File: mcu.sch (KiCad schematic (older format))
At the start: 21 parts, among them J5 CONN_01X03, J6 CONN_01X06, J7 CONN_01X03, SW1 SW_Push, U6 STM32L476RG, Y1 ABS07-120-32.768kHz-T

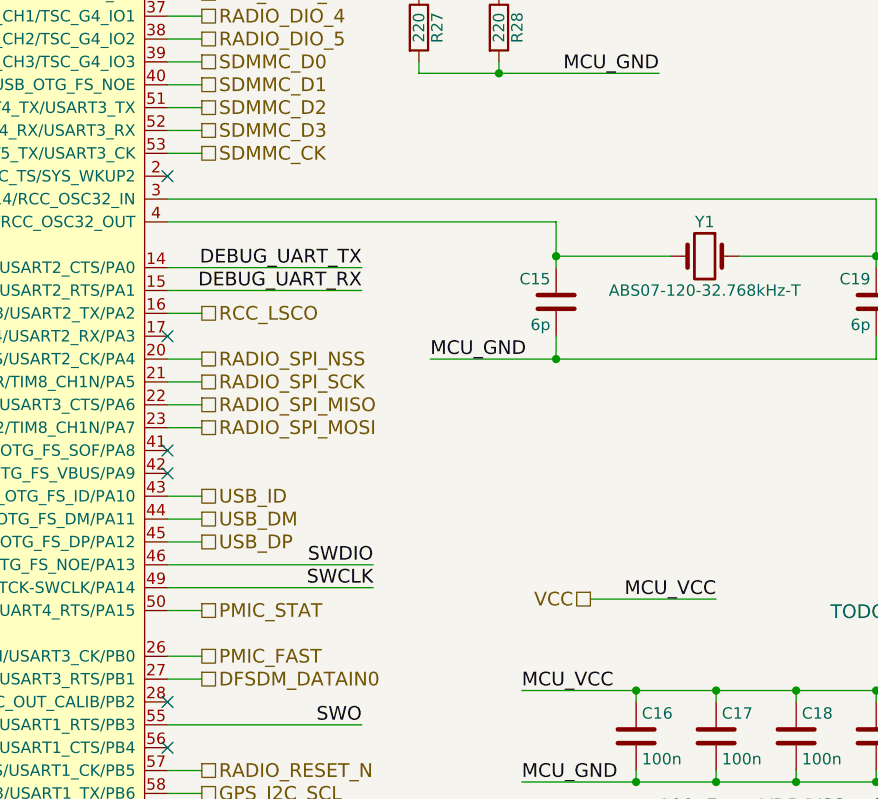
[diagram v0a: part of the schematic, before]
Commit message: Most components arranged on PCB
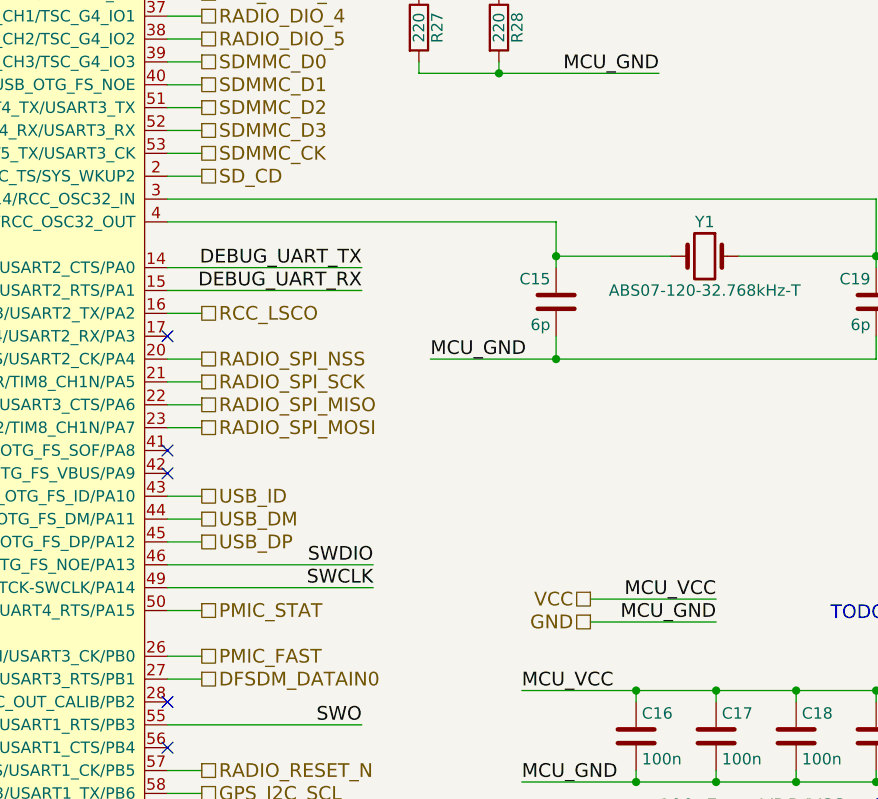
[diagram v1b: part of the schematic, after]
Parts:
- C22: footprint (none) -> Capacitors_SMD:C_0805_HandSoldering
- J6: footprint Pin_Headers:Pin_Header_Straight_1x06_Pitch2.54mm -> tracking_device:Pin_Header_Straight_1x06_Pitch2.54mm
- J7: footprint Pin_Headers:Pin_Header_Straight_1x03_Pitch2.54mm -> tracking_device:Pin_Header_Straight_1x03_Pitch2.54mm
- U6: footprint LQFP64 -> Housings_QFP:LQFP-64_10x10mm_Pitch0.5mm
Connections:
- net MCU_GND is gone; now on net GND: C15.2, C16.2, C17.2, C18.2, C19.2, C20.2, C21.2, C22.2, J5.3 (P3), J7.3 (P3), R26.2, R27.2, R28.2, SW1.2, U6.12 (VSSA), U6.18 (VSS), U6.31 (VSS), U6.47 (VSS), U6.63 (VSS)
- net SD_CD: now reaches U6.2 (PC13/RTC_OUT_ALARM/RTC_OUT_CALIB/RTC_TAMP1/RTC_TS/SYS_WKUP2)
- no-connect marks 14 -> 13
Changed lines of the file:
@@
 LIBS:battery_management
 LIBS:ESD_Protection
+LIBS:u-blox
 LIBS:tracking_device
-LIBS:u-blox
 LIBS:tracking_device-cache
 EELAYER 25 0
@@
 F 0 "J6" H 12150 1650 50  0000 C CNN
 F 1 "CONN_01X06" V 12250 1300 50  0000 C CNN
-F 2 "Pin_Headers:Pin_Header_Straight_1x06_Pitch2.54mm" H 12150 1300 50  0001 C CNN
+F 2 "tracking_device:Pin_Header_Straight_1x06_Pitch2.54mm" H 12150 1300 50  0001 C CNN
 F 3 "" H 12150 1300 50  0001 C CNN
 	1    12150 1300
@@
 F 0 "J7" H 12400 3200 50  0000 C CNN
 F 1 "CONN_01X03" V 12500 3000 50  0000 C CNN
-F 2 "Pin_Headers:Pin_Header_Straight_1x03_Pitch2.54mm" H 12400 3000 50  0001 C CNN
+F 2 "tracking_device:Pin_Header_Straight_1x03_Pitch2.54mm" H 12400 3000 50  0001 C CNN
 F 3 "" H 12400 3000 50  0001 C CNN
 	1    12400 3000
@@
 F 0 "U6" H 700 7450 50  0000 L BNN
 F 1 "STM32L476RG" H 7600 7450 50  0000 R BNN
-F 2 "LQFP64" H 7550 7350 50  0001 R TNN
+F 2 "Housings_QFP:LQFP-64_10x10mm_Pitch0.5mm" H 7550 7350 50  0001 R TNN
 F 3 "" H 3500 4700 50  0001 C CNN
 	1    4200 4400
@@
 F 0 "C22" H 11675 6200 50  0000 L CNN
 F 1 "4.7u" H 11675 6000 50  0000 L CNN
-F 2 "" H 11688 5950 50  0001 C CNN
+F 2 "Capacitors_SMD:C_0805_HandSoldering" H 11688 5950 50  0001 C CNN
 F 3 "" H 11650 6100 50  0001 C CNN
 	1    11650 6100
@@
 NoConn ~ 7850 1850
 NoConn ~ 7850 1950
-NoConn ~ 7850 3650
 NoConn ~ 7850 6150
 Text HLabel 8000 4250 2    60   UnSpc ~ 0
@@
 NoConn ~ 2450 3350
 NoConn ~ 2300 3050
+Text HLabel 8000 3650 2    60   UnSpc ~ 0
+SD_CD
+Wire Wire Line
+	8000 3650 7850 3650
+Text HLabel 9700 5600 0    60   UnSpc ~ 0
+GND
+Text Label 10250 5600 2    60   ~ 0
+MCU_GND
+Wire Wire Line
+	10250 5600 9700 5600
 $EndSCHEMATC

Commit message: Version sent out for fabrication
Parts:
- removed J5: CONN_01X03, Pin_Headers:Pin_Header_Straight_1x03_Pitch2.54mm, symbol CONN_01X03
- renumbered J7 to J10, J6 to J9, R24 to R26, R25 to R27, R26 to R28, R27 to R29, R28 to R30, SW1 to SW3
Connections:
- net PMIC_FAST: now also U6.42 (DAC1_EXTI9/LCD_COM1/TIM15_BKIN/TIM1_CH2/USART1_TX/USB_OTG_FS_VBUS/PA9); no longer U6.26 (ADC1_IN15/ADC2_IN15/COMP1_OUT/LCD_SEG5/OPAMP2_VOUT/QUADSPI_BK1_IO1/TIM1_CH2N/TIM3_CH3/TIM8_CH2N/USART3_CK/PB0)
- net SWITCH_1: now reaches U6.11 (PC3/ADC1_IN4/ADC2_IN4/ADC3_IN4/LCD_VLCD/LPTIM1_ETR/LPTIM2_ETR/SAI1_SD_A/SPI2_MOSI)
- net SWITCH_2: now reaches U6.17 (ADC1_IN8/ADC2_IN8/LCD_SEG2/OPAMP1_VOUT/TIM15_CH2/TIM2_CH4/TIM5_CH4/USART2_RX/PA3)
- net GPS_EXTINT: now reaches U6.28 (COMP1_INP/DFSDM_CKIN0/I2C3_SMBA/LPTIM1_OUT/RTC_OUT_ALARM/RTC_OUT_CALIB/PB2)
- net VUSB_DET: now reaches U6.33 (DFSDM_DATIN1/I2C2_SMBA/LCD_SEG12/LPUART1_DE/LPUART1_RTS/SAI2_FS_A/SPI2_NSS/SWPMI1_IO/TIM15_BKIN/TIM1_BKIN/TIM1_BKIN_COMP2/TSC_G1_IO1/USART3_CK/PB12)
- net GPS_TIMEPULSE: now reaches U6.36 (ADC1_EXTI15/ADC2_EXTI15/ADC3_EXTI15/DFSDM_CKIN2/LCD_SEG15/RTC_REFIN/SAI2_SD_A/SPI2_MOSI/SWPMI1_SUSPEND/TIM15_CH2/TIM1_CH3N/TIM8_CH3N/TSC_G1_IO4/PB15)
- net GPS_RESET_N: now reaches U6.56 (COMP2_INP/LCD_SEG8/SAI1_MCLK_B/SPI1_MISO/SPI3_MISO/SYS_JTRST/TIM17_BKIN/TIM3_CH1/TSC_G2_IO1/UART5_DE/UART5_RTS/USART1_CTS/PB4)
- no-connect marks 13 -> 6
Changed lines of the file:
@@
 LIBS:tracking_device
 LIBS:RF_Modules
+LIBS:Electromechanical
+LIBS:Test_Point
+LIBS:electomech-misc
+LIBS:_electromech
+LIBS:Mounting_Hole
 LIBS:tracking_device-cache
 EELAYER 25 0
@@
 RADIO_SPI_NSS
 $Comp
-L CONN_01X06 J6
+L CONN_01X06 J9
 U 1 1 59A76B28
 P 12150 1300
-F 0 "J6" H 12150 1650 50  0000 C CNN
+F 0 "J9" H 12150 1650 50  0000 C CNN
 F 1 "CONN_01X06" V 12250 1300 50  0000 C CNN
 F 2 "tracking_device:Pin_Header_Straight_1x06_Pitch2.54mm" H 12150 1300 50  0001 C CNN
@@
 $EndComp
 $Comp
-L CONN_01X03 J7
+L CONN_01X03 J10
 U 1 1 59A77202
 P 12400 3000
-F 0 "J7" H 12400 3200 50  0000 C CNN
+F 0 "J10" H 12400 3200 50  0000 C CNN
 F 1 "CONN_01X03" V 12500 3000 50  0000 C CNN
 F 2 "tracking_device:Pin_Header_Straight_1x03_Pitch2.54mm" H 12400 3000 50  0001 C CNN
@@
 Text Label 9000 4450 0    60   ~ 0
 MCU_GND
-$Comp
-L STM32L476RG U6
-U 1 1 59B8C0F3
-P 4200 4400
-F 0 "U6" H 700 7450 50  0000 L BNN
-F 1 "STM32L476RG" H 7600 7450 50  0000 R BNN
-F 2 "Housings_QFP:LQFP-64_10x10mm_Pitch0.5mm" H 7550 7350 50  0001 R TNN
-F 3 "" H 3500 4700 50  0001 C CNN
-	1    4200 4400
-	-1   0    0    -1
-$EndComp
 Text HLabel 8000 3350 2    60   UnSpc ~ 0
 SDMMC_D2
@@
 USB_ID
 $Comp
-L R R25
+L R R27
 U 1 1 59BE1ED5
 P 8800 1350
-F 0 "R25" V 8880 1350 50  0000 C CNN
+F 0 "R27" V 8880 1350 50  0000 C CNN
 F 1 "DNI" V 8800 1350 50  0000 C CNN
 F 2 "Resistors_SMD:R_0805_HandSoldering" V 8730 1350 50  0001 C CNN
@@
 MCU_VCC
 $Comp
-L R R26
+L R R28
 U 1 1 59BE220F
 P 8800 1750
-F 0 "R26" V 8880 1750 50  0000 C CNN
+F 0 "R28" V 8880 1750 50  0000 C CNN
 F 1 "0" V 8800 1750 50  0000 C CNN
 F 2 "Resistors_SMD:R_0805_HandSoldering" V 8730 1750 50  0001 C CNN
@@
 Text Label 8750 5350 2    60   ~ 0
 SWDIO
-$Comp
-L CONN_01X03 J5
-U 1 1 59BE7C26
-P 9250 1550
-F 0 "J5" H 9250 1750 50  0000 C CNN
-F 1 "CONN_01X03" V 9350 1550 50  0000 C CNN
-F 2 "Pin_Headers:Pin_Header_Straight_1x03_Pitch2.54mm" H 9250 1550 50  0001 C CNN
-F 3 "" H 9250 1550 50  0001 C CNN
-	1    9250 1550
-	1    0    0    -1
-$EndComp
 Text HLabel 8000 1650 2    60   UnSpc ~ 0
 VBAT
@@
 	9700 5500 10250 5500
 Wire Wire Line
-	8700 1550 9050 1550
-Wire Wire Line
 	9550 4000 10050 4000
 Wire Wire Line
@@
 Wire Wire Line
 	8800 1950 8800 1900
-Wire Wire Line
-	8800 1150 9050 1150
-Wire Wire Line
-	9050 1150 9050 1450
 Connection ~ 8800 1150
-Wire Wire Line
-	9050 1650 9050 1950
 Wire Wire Line
 	8000 1650 7850 1650
@@
 NoConn ~ 7850 1850
 NoConn ~ 7850 1950
-NoConn ~ 7850 6150
 Text HLabel 8000 4250 2    60   UnSpc ~ 0
 RCC_LSCO
 Wire Wire Line
 	8000 4250 7850 4250
-NoConn ~ 7850 4350
-NoConn ~ 11050 3700
 $Comp
 L LED D2
@@
 $EndComp
 $Comp
-L R R28
+L R R30
 U 1 1 59BF19BB
 P 9300 3000
-F 0 "R28" V 9380 3000 50  0000 C CNN
+F 0 "R30" V 9380 3000 50  0000 C CNN
 F 1 "220" V 9300 3000 50  0000 C CNN
 F 2 "Resistors_SMD:R_0805_HandSoldering" V 9230 3000 50  0001 C CNN
@@
 Wire Wire Line
 	8950 2450 7850 2450
-NoConn ~ 7850 5950
-$Comp
-L R R24
+$Comp
+L R R26
 U 1 1 59BF23D1
 P 8550 1550
-F 0 "R24" V 8630 1550 50  0000 C CNN
+F 0 "R26" V 8630 1550 50  0000 C CNN
 F 1 "10k" V 8550 1550 50  0000 C CNN
 F 2 "Resistors_SMD:R_0805_HandSoldering" V 8480 1550 50  0001 C CNN
@@
 	8000 6250 7850 6250
 $Comp
-L SW_Push SW1
+L SW_Push SW3
 U 1 1 59C0698A
 P 11550 2100
-F 0 "SW1" H 11600 2200 50  0000 L CNN
+F 0 "SW3" H 11600 2200 50  0000 L CNN
 F 1 "SW_Push" H 11550 2040 50  0000 C CNN
 F 2 "Buttons_Switches_THT:SW_PUSH_6mm" H 11550 2300 50  0001 C CNN
@@
 	10950 4450 10950 4350
 $Comp
-L R R27
+L R R29
 U 1 1 59C07A6F
 P 8950 3000
-F 0 "R27" V 9030 3000 50  0000 C CNN
+F 0 "R29" V 9030 3000 50  0000 C CNN
 F 1 "220" V 8950 3000 50  0000 C CNN
 F 2 "Resistors_SMD:R_0805_HandSoldering" V 8880 3000 50  0001 C CNN
@@
 	1    0    0    -1
 $EndComp
-NoConn ~ 7850 4850
-NoConn ~ 7850 4950
 Text Label 8700 4050 2    60   ~ 0
 DEBUG_UART_TX
@@
 	0    -1   -1   0
 $EndComp
-NoConn ~ 7850 2650
 Text HLabel 8000 2950 2    60   UnSpc ~ 0
 RADIO_DIO_4
@@
 Text HLabel 8000 7150 2    60   UnSpc ~ 0
 PMIC_I2C_SDA
-NoConn ~ 7850 6950
-NoConn ~ 7850 7250
 Text HLabel 8000 5550 2    60   UnSpc ~ 0
 PMIC_STAT
-Text HLabel 8000 5750 2    60   UnSpc ~ 0
+Text HLabel 8000 4950 2    60   UnSpc ~ 0
 PMIC_FAST
 Wire Wire Line
 	8000 5550 7850 5550
-Wire Wire Line
-	7850 5750 8000 5750
 NoConn ~ 2450 3350
 NoConn ~ 2300 3050
@@
 Wire Wire Line
 	10250 5600 9700 5600
+Text HLabel 8000 2650 2    60   UnSpc ~ 0
+SWITCH_1
+Text HLabel 8000 4350 2    60   UnSpc ~ 0
+SWITCH_2
+Wire Wire Line
+	8800 1550 8700 1550
+$Comp
+L STM32L476RG U6
+U 1 1 59B8C0F3
+P 4200 4400
+F 0 "U6" H 700 7450 50  0000 L BNN
+F 1 "STM32L476RG" H 7600 7450 50  0000 R BNN
+F 2 "Housings_QFP:LQFP-64_10x10mm_Pitch0.5mm" H 7550 7350 50  0001 R TNN
+F 3 "" H 3500 4700 50  0001 C CNN
+	1    4200 4400
+	-1   0    0    -1
+$EndComp
+Wire Wire Line
+	8000 4350 7850 4350
+NoConn ~ 7850 4850
+Wire Wire Line
+	7850 2650 8000 2650
+Text HLabel 8000 6950 2    60   UnSpc ~ 0
+VUSB_DET
+Wire Wire Line
+	8000 6950 7850 6950
+Text HLabel 8000 5950 2    60   UnSpc ~ 0
+GPS_EXTINT
+Text HLabel 8000 6150 2    60   UnSpc ~ 0
+GPS_RESET_N
+Wire Wire Line
+	8000 5950 7850 5950
+Wire Wire Line
+	7850 6150 8000 6150
+Text HLabel 8000 7250 2    60   UnSpc ~ 0
+GPS_TIMEPULSE
+Wire Wire Line
+	7850 7250 8000 7250
+Wire Wire Line
+	8000 4950 7850 4950
+NoConn ~ 7850 5750
 $EndSCHEMATC

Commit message: Rev 1 sent for fabrication
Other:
- note removed: "TODO: connect debug interface to connector in this page\n"
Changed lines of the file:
@@
 encoding utf-8
 Sheet 2 3
-Title ""
+Title "Microcontroller"
 Date ""
-Rev ""
+Rev "1"
 Comp ""
 Comment1 ""
@@
 Text HLabel 8000 4550 2    60   UnSpc ~ 0
 RADIO_SPI_SCK
-Text Notes 10750 5600 0    60   ~ 0
-TODO: connect debug interface to connector in this page\n
 Text Label 8700 6050 2    60   ~ 0
 SWO

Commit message: Working on rev 3, started board layout
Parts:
- removed R26: 10k, Resistors_SMD:R_0805_HandSoldering, symbol R
- removed R27: DNI, Resistors_SMD:R_0805_HandSoldering, symbol R
- removed R28: 0, Resistors_SMD:R_0805_HandSoldering, symbol R
- added C13: 100n, Capacitors_SMD:C_0805_HandSoldering, symbol C
- added R17: 10k, Resistors_SMD:R_0805_HandSoldering, symbol R
- renumbered C15 to C14, C16 to C15, C17 to C16, C18 to C17, C19 to C18, C20 to C19, C21 to C20, C22 to C21, D2 to D3, D3 to D4, J9 to J8, J10 to J9, R29 to R18, R30 to R19
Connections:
- net GND: now also U6.60 (BOOT0), C13.2
- net NRST: now also C13.1, R17.2
- net VDD: now also R17.1
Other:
- moved on the sheet: SW3
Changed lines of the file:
@@
 RADIO_SPI_NSS
 $Comp
-L CONN_01X06 J9
+L CONN_01X06 J8
 U 1 1 59A76B28
 P 12150 1300
-F 0 "J9" H 12150 1650 50  0000 C CNN
+F 0 "J8" H 12150 1650 50  0000 C CNN
 F 1 "CONN_01X06" V 12250 1300 50  0000 C CNN
 F 2 "tracking_device:Pin_Header_Straight_1x06_Pitch2.54mm" H 12150 1300 50  0001 C CNN
@@
 $EndComp
 $Comp
-L CONN_01X03 J10
+L CONN_01X03 J9
 U 1 1 59A77202
 P 12400 3000
-F 0 "J10" H 12400 3200 50  0000 C CNN
+F 0 "J9" H 12400 3200 50  0000 C CNN
 F 1 "CONN_01X03" V 12500 3000 50  0000 C CNN
 F 2 "tracking_device:Pin_Header_Straight_1x03_Pitch2.54mm" H 12400 3000 50  0001 C CNN
@@
 DEBUG_UART_RX
 $Comp
-L C C16
+L C C15
 U 1 1 59A77466
 P 9900 6100
-F 0 "C16" H 9925 6200 50  0000 L CNN
+F 0 "C15" H 9925 6200 50  0000 L CNN
 F 1 "100n" H 9925 6000 50  0000 L CNN
 F 2 "Capacitors_SMD:C_0805_HandSoldering" H 9938 5950 50  0001 C CNN
@@
 $EndComp
 $Comp
-L C C15
+L C C14
 U 1 1 59B38E77
 P 9550 4200
-F 0 "C15" H 9575 4300 50  0000 L CNN
+F 0 "C14" H 9575 4300 50  0000 L CNN
 F 1 "6p" H 9575 4100 50  0000 L CNN
 F 2 "Capacitors_SMD:C_0805_HandSoldering" H 9588 4050 50  0001 C CNN
@@
 Text HLabel 8000 5050 2    60   UnSpc ~ 0
 USB_ID
-$Comp
-L R R27
-U 1 1 59BE1ED5
-P 8800 1350
-F 0 "R27" V 8880 1350 50  0000 C CNN
-F 1 "DNI" V 8800 1350 50  0000 C CNN
-F 2 "Resistors_SMD:R_0805_HandSoldering" V 8730 1350 50  0001 C CNN
-F 3 "" H 8800 1350 50  0001 C CNN
-	1    8800 1350
-	-1   0    0    1
-$EndComp
-Text Label 8800 700  3    60   ~ 0
-MCU_VCC
-$Comp
-L R R28
-U 1 1 59BE220F
-P 8800 1750
-F 0 "R28" V 8880 1750 50  0000 C CNN
-F 1 "0" V 8800 1750 50  0000 C CNN
-F 2 "Resistors_SMD:R_0805_HandSoldering" V 8730 1750 50  0001 C CNN
-F 3 "" H 8800 1750 50  0001 C CNN
-	1    8800 1750
-	1    0    0    -1
-$EndComp
 Text HLabel 8000 4550 2    60   UnSpc ~ 0
 RADIO_SPI_SCK
@@
 Text HLabel 8000 1650 2    60   UnSpc ~ 0
 VBAT
-Text Label 9550 1950 2    60   ~ 0
-MCU_GND
-Text Label 10950 2100 0    60   ~ 0
-NRST
+Text Label 8400 1550 2    60   ~ 0
+MCU_GND
 Wire Wire Line
 	8000 6550 7850 6550
@@
 Connection ~ 10950 6300
 Wire Wire Line
-	7850 1450 8400 1450
+	7850 1450 8750 1450
 Wire Wire Line
 	9700 5500 10250 5500
@@
 	8000 5050 7850 5050
 Wire Wire Line
-	8800 1500 8800 1600
-Wire Wire Line
-	8800 700  8800 1200
-Connection ~ 8800 1550
-Wire Wire Line
 	7850 7050 8000 7050
 Wire Wire Line
@@
 	8750 5350 7850 5350
 Wire Wire Line
-	8800 1950 8800 1900
-Connection ~ 8800 1150
-Wire Wire Line
 	8000 1650 7850 1650
-Wire Wire Line
-	8800 1950 9550 1950
-Connection ~ 9050 1950
 Wire Wire Line
 	4250 1300 4250 1000
@@
 	4000 1000 4000 1300
 Connection ~ 4000 1000
-Text Label 12300 2100 2    60   ~ 0
+Text Label 9700 1450 2    60   ~ 0
 MCU_GND
 Text Notes 11000 6450 2    60   ~ 0
 100nF per VDD/VSS pair
 $Comp
-L C C22
+L C C21
 U 1 1 59BF0662
 P 11650 6100
-F 0 "C22" H 11675 6200 50  0000 L CNN
+F 0 "C21" H 11675 6200 50  0000 L CNN
 F 1 "4.7u" H 11675 6000 50  0000 L CNN
 F 2 "Capacitors_SMD:C_0805_HandSoldering" H 11688 5950 50  0001 C CNN
@@
 	8000 4250 7850 4250
 $Comp
-L LED D2
+L LED D3
 U 1 1 59BF17F5
 P 8950 2600
-F 0 "D2" H 8950 2700 50  0000 C CNN
+F 0 "D3" H 8950 2700 50  0000 C CNN
 F 1 "LED" H 8950 2500 50  0000 C CNN
 F 2 "LEDs:LED_0805_HandSoldering" H 8950 2600 50  0001 C CNN
@@
 $EndComp
 $Comp
-L R R30
+L R R19
 U 1 1 59BF19BB
 P 9300 3000
-F 0 "R30" V 9380 3000 50  0000 C CNN
+F 0 "R19" V 9380 3000 50  0000 C CNN
 F 1 "220" V 9300 3000 50  0000 C CNN
 F 2 "Resistors_SMD:R_0805_HandSoldering" V 9230 3000 50  0001 C CNN
@@
 Wire Wire Line
 	8950 2450 7850 2450
-$Comp
-L R R26
-U 1 1 59BF23D1
-P 8550 1550
-F 0 "R26" V 8630 1550 50  0000 C CNN
-F 1 "10k" V 8550 1550 50  0000 C CNN
-F 2 "Resistors_SMD:R_0805_HandSoldering" V 8480 1550 50  0001 C CNN
-F 3 "" H 8550 1550 50  0001 C CNN
-	1    8550 1550
-	0    -1   -1   0
-$EndComp
 Wire Wire Line
 	8400 1550 7850 1550
@@
 L SW_Push SW3
 U 1 1 59C0698A
-P 11550 2100
-F 0 "SW3" H 11600 2200 50  0000 L CNN
-F 1 "SW_Push" H 11550 2040 50  0000 C CNN
-F 2 "Buttons_Switches_THT:SW_PUSH_6mm" H 11550 2300 50  0001 C CNN
-F 3 "" H 11550 2300 50  0001 C CNN
-	1    11550 2100
-	1    0    0    -1
-$EndComp
-Wire Wire Line
-	11350 2100 10950 2100
-Wire Wire Line
-	11750 2100 12300 2100
+P 8950 1450
+F 0 "SW3" H 9000 1550 50  0000 L CNN
+F 1 "SW_Push" H 8950 1390 50  0000 C CNN
+F 2 "Buttons_Switches_THT:SW_PUSH_6mm" H 8950 1650 50  0001 C CNN
+F 3 "" H 8950 1650 50  0001 C CNN
+	1    8950 1450
+	1    0    0    -1
+$EndComp
+Wire Wire Line
+	9150 1450 9700 1450
 Wire Wire Line
 	10950 3750 10950 4050
@@
 	10950 4450 10950 4350
 $Comp
-L R R29
+L R R18
 U 1 1 59C07A6F
 P 8950 3000
-F 0 "R29" V 9030 3000 50  0000 C CNN
+F 0 "R18" V 9030 3000 50  0000 C CNN
 F 1 "220" V 8950 3000 50  0000 C CNN
 F 2 "Resistors_SMD:R_0805_HandSoldering" V 8880 3000 50  0001 C CNN
@@
 	11400 2900 12200 2900
 $Comp
-L C C19
+L C C18
 U 1 1 59C089D0
 P 10950 4200
-F 0 "C19" H 10975 4300 50  0000 L CNN
+F 0 "C18" H 10975 4300 50  0000 L CNN
 F 1 "6p" H 10975 4100 50  0000 L CNN
 F 2 "Capacitors_SMD:C_0805_HandSoldering" H 10988 4050 50  0001 C CNN
@@
 $EndComp
 $Comp
-L C C17
+L C C16
 U 1 1 59C09613
 P 10250 6100
-F 0 "C17" H 10275 6200 50  0000 L CNN
+F 0 "C16" H 10275 6200 50  0000 L CNN
 F 1 "100n" H 10275 6000 50  0000 L CNN
 F 2 "Capacitors_SMD:C_0805_HandSoldering" H 10288 5950 50  0001 C CNN
@@
 $EndComp
 $Comp
-L C C18
+L C C17
 U 1 1 59C09660
 P 10600 6100
-F 0 "C18" H 10625 6200 50  0000 L CNN
+F 0 "C17" H 10625 6200 50  0000 L CNN
 F 1 "100n" H 10625 6000 50  0000 L CNN
 F 2 "Capacitors_SMD:C_0805_HandSoldering" H 10638 5950 50  0001 C CNN
@@
 $EndComp
 $Comp
-L C C20
+L C C19
 U 1 1 59C096AC
 P 10950 6100
-F 0 "C20" H 10975 6200 50  0000 L CNN
+F 0 "C19" H 10975 6200 50  0000 L CNN
 F 1 "100n" H 10975 6000 50  0000 L CNN
 F 2 "Capacitors_SMD:C_0805_HandSoldering" H 10988 5950 50  0001 C CNN
@@
 $EndComp
 $Comp
-L C C21
+L C C20
 U 1 1 59C096FD
 P 11300 6100
-F 0 "C21" H 11325 6200 50  0000 L CNN
+F 0 "C20" H 11325 6200 50  0000 L CNN
 F 1 "100n" H 11325 6000 50  0000 L CNN
 F 2 "Capacitors_SMD:C_0805_HandSoldering" H 11338 5950 50  0001 C CNN
@@
 $EndComp
 $Comp
-L LED D3
+L LED D4
 U 1 1 59C09B57
 P 9300 2600
-F 0 "D3" H 9300 2700 50  0000 C CNN
+F 0 "D4" H 9300 2700 50  0000 C CNN
 F 1 "LED" H 9300 2500 50  0000 C CNN
 F 2 "LEDs:LED_0805_HandSoldering" H 9300 2600 50  0001 C CNN
@@
 Text HLabel 8000 4350 2    60   UnSpc ~ 0
 SWITCH_2
-Wire Wire Line
-	8800 1550 8700 1550
 $Comp
 L STM32L476RG U6
@@
 	8000 4950 7850 4950
 NoConn ~ 7850 5750
+$Comp
+L R R17
+U 1 1 5ACBFB3F
+P 8550 1150
+F 0 "R17" V 8630 1150 50  0000 C CNN
+F 1 "10k" V 8550 1150 50  0000 C CNN
+F 2 "Resistors_SMD:R_0805_HandSoldering" V 8480 1150 50  0001 C CNN
+F 3 "" H 8550 1150 50  0001 C CNN
+	1    8550 1150
+	1    0    0    -1
+$EndComp
+$Comp
+L C C13
+U 1 1 5ACBFBD9
+P 8600 1650
+F 0 "C13" H 8625 1750 50  0000 L CNN
+F 1 "100n" H 8625 1550 50  0000 L CNN
+F 2 "Capacitors_SMD:C_0805_HandSoldering" H 8638 1500 50  0001 C CNN
+F 3 "" H 8600 1650 50  0001 C CNN
+	1    8600 1650
+	1    0    0    -1
+$EndComp
+Wire Wire Line
+	8600 1450 8600 1500
+Connection ~ 8600 1450
+Wire Wire Line
+	8550 1300 8550 1450
+Connection ~ 8550 1450
+Text Label 8300 1000 0    60   ~ 0
+VDD
+Wire Wire Line
+	8300 1000 8550 1000
+Text Label 9100 1900 2    60   ~ 0
+MCU_GND
+Wire Wire Line
+	9100 1900 8600 1900
+Wire Wire Line
+	8600 1900 8600 1800
 $EndSCHEMATC
